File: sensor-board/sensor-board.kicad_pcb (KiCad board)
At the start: 2 copper layers, 11 parts, among them Q1 DMG3415U-7, U1 MCP73831-3-OT, U2 Arduino-nano-BLE-33, U3 SCD40-D-R2, U4 SGP40-D-R4

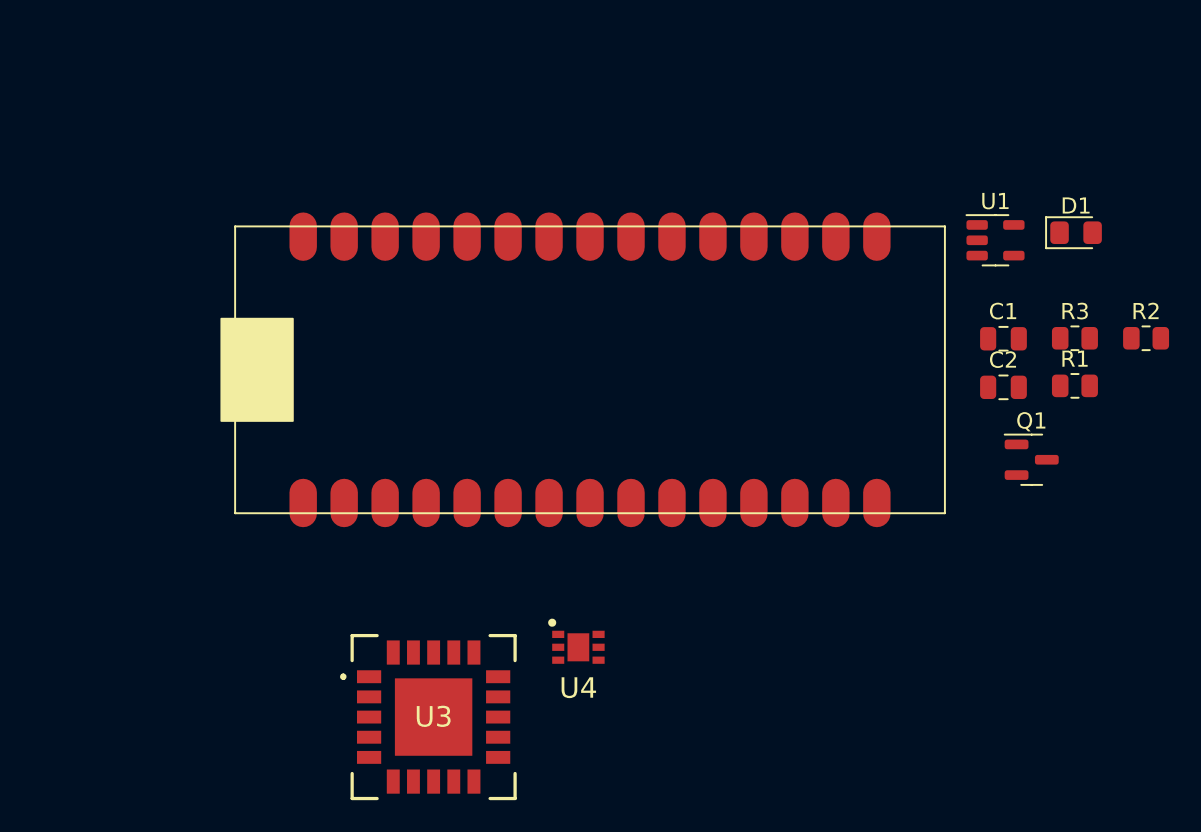
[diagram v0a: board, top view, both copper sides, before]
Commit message: update sensors and sensorBoard
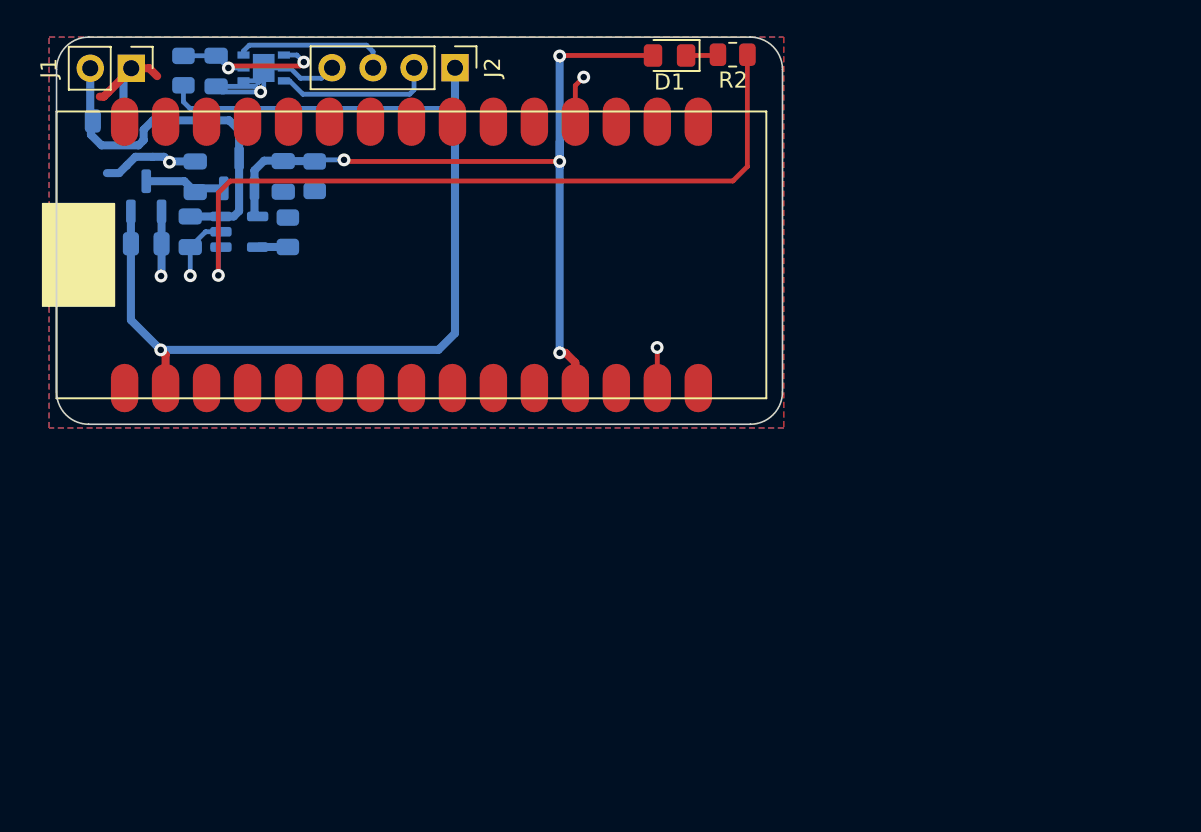
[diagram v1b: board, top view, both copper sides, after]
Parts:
- added C3: 10uF, Capacitor_SMD:C_0805_2012Metric, B.Cu at (134.1, 64.6)
- added C4: 10uF, Capacitor_SMD:C_0805_2012Metric, B.Cu at (123.2, 61.2)
- added C5: 10uF, Capacitor_SMD:C_0805_2012Metric, B.Cu at (125.6, 68.8)
- added C6: 1uF, Capacitor_SMD:C_0805_2012Metric, B.Cu at (129.9, 58.1)
- added J1: Batt, Connector_PinHeader_2.54mm:PinHeader_1x02_P2.54mm_Vertical, F.Cu at (124.6, 57.9)
- added J2: I2C, Connector_PinHeader_2.54mm:PinHeader_1x04_P2.54mm_Vertical, F.Cu at (144.7, 57.9)
- added R4: 4.7R, Resistor_SMD:R_0805_2012Metric, B.Cu at (127.9, 58.1)
- C1, C2, Q1, R1, R3, U1, U4: moved to B.Cu
- U3: value SCD40-D-R2 -> MCP1700T-3102; footprint hack-it-back:SCD40DR2 -> Package_TO_SOT_SMD:SOT-23; moved to B.Cu
- moved Q1 52.2 mm to (131.3, 64.4), turned to 90 degrees
- moved C2 51.8 mm to (128.6, 64.7), turned to 90 degrees
- moved C1 50.8 mm to (128.3, 68.1), turned to -90 degrees
- moved R1 49.7 mm to (134.3, 68.1), turned to 90 degrees
- moved R3 48.2 mm to (136.0, 64.6), turned to -90 degrees
- moved U1 46.9 mm to (131.3, 68.1)
- moved U4 40.9 mm to (132.8, 57.9), turned to 180 degrees
- moved U3 36.9 mm to (125.6, 65.9), turned to 90 degrees
- moved R2 31.1 mm to (161.9, 57.1), turned to 180 degrees
- moved D1 27.5 mm to (158.0, 57.1), turned to 180 degrees
- moved U2 13.2 mm to (142.0, 69.5)
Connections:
- U2 pad 15: VDD -> unconnected-(U2-Pad15)
- U2 pad 19: unconnected-(U2-Pad19) -> GND
- U2 pad 2: unconnected-(U2-Pad2) -> +3V3
- U3 pad 1: (no net) -> GND
- U3 pad 2: (no net) -> +3V3
- U3 pad 3: (no net) -> VDD
- U4 pad 1: unconnected-(U4-Pad1) -> Net-(U4-Pad1)
- U4 pad 2: unconnected-(U4-Pad2) -> GND
- U4 pad 3: unconnected-(U4-Pad3) -> /SDA
- U4 pad 4: unconnected-(U4-Pad4) -> GND
- U4 pad 5: unconnected-(U4-Pad5) -> Net-(U4-Pad1)
- U4 pad 6: unconnected-(U4-Pad6) -> /SCL
- U4 pad 7: unconnected-(U4-Pad7) -> GND
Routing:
- net +3V3: track 0.00 -> 67.8 mm, vias 0 -> 1
- net VBUS: track 0.00 -> 57.3 mm, vias 0 -> 4
- net Net-(R2-Pad1): track 0.00 -> 47.3 mm, vias 0 -> 1
- net GND: track 0.00 -> 41.8 mm, vias 0 -> 6
- net +BATT: track 0.00 -> 23.2 mm
- net Net-(U4-Pad1): track 0.00 -> 10.3 mm, vias 0 -> 2
- net /SDA: track 0.00 -> 9.89 mm
- net /SCL: track 0.00 -> 9.60 mm
- net VDD: track 0.00 -> 5.18 mm
- net Net-(D1-Pad1): track 0.00 -> 2.00 mm
- net Net-(R1-Pad1): track 0.00 -> 1.88 mm
- added copper zone on B.Cu, net GND
- added copper zone on F.Cu, net GND
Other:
- board outline added: 45 x 24 mm

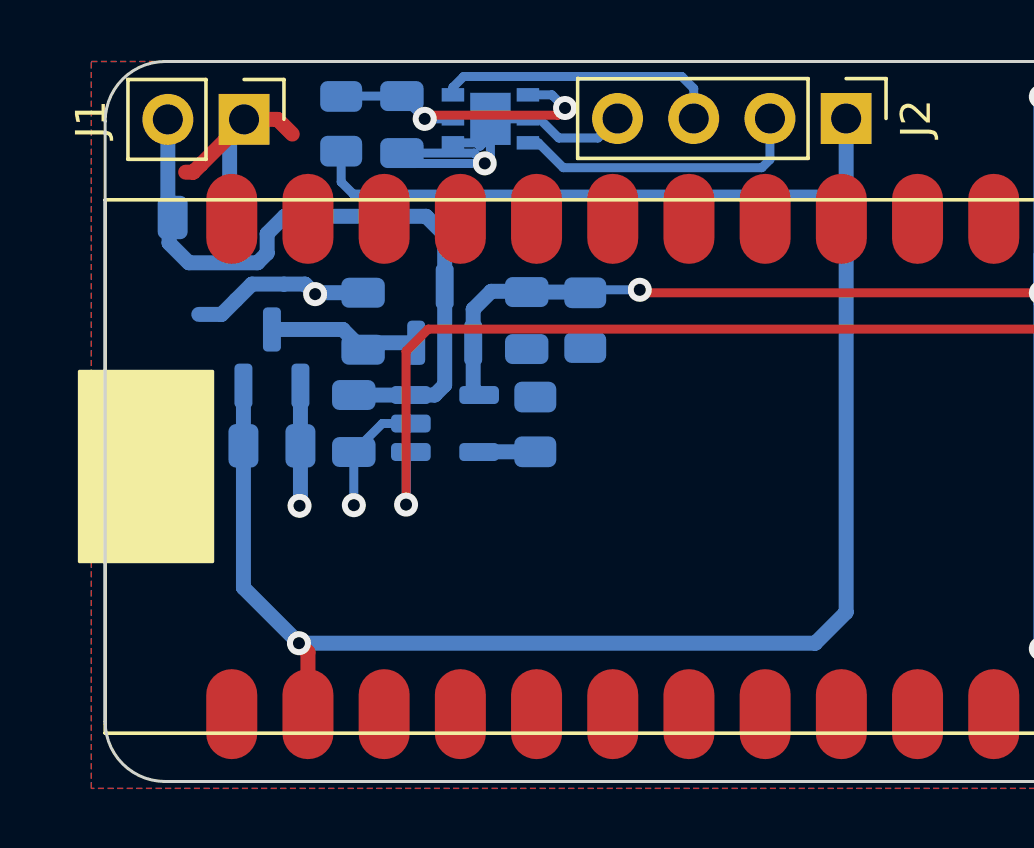
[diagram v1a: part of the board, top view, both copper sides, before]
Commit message: update pins sensor board
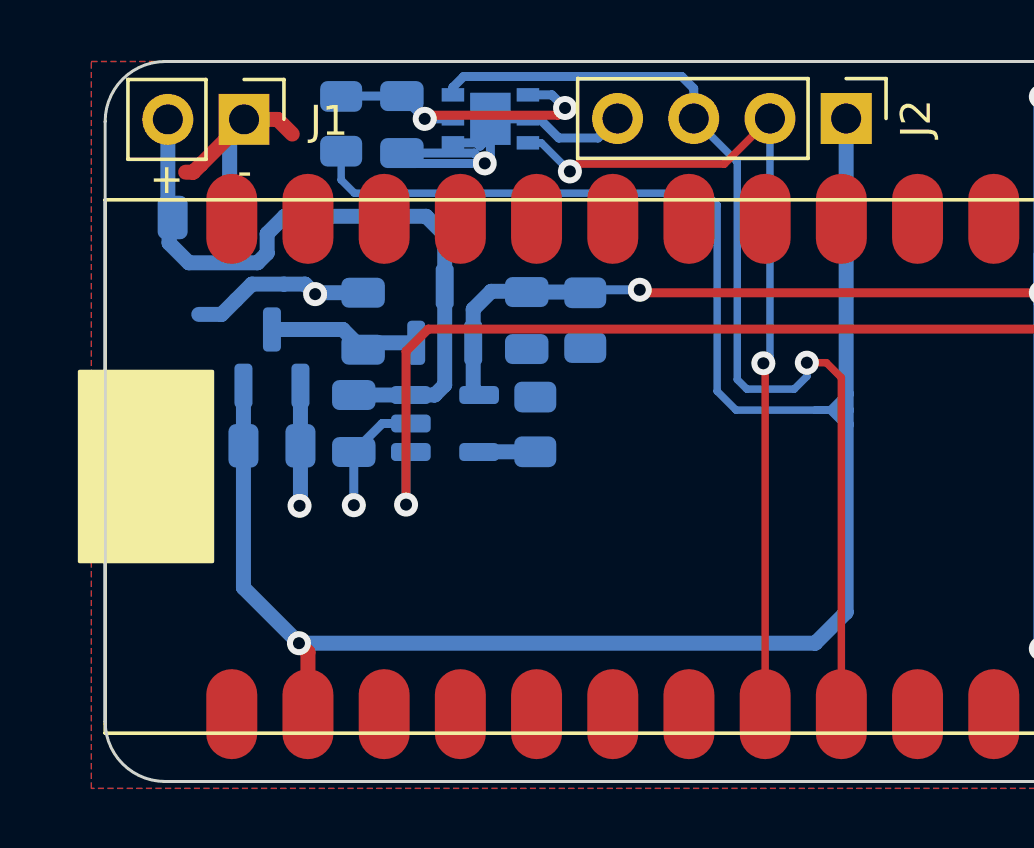
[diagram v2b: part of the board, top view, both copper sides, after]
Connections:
- U2 pad 8: unconnected-(U2-Pad8) -> /SDA
- U2 pad 9: unconnected-(U2-Pad9) -> /SCL
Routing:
- net /SCL: track 9.60 -> 34.6 mm, vias 0 -> 1
- net /SDA: track 9.89 -> 29.2 mm, vias 0 -> 2
- net +3V3: track 67.8 -> 75.6 mm
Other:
- board text added: "+"
- board text added: "-"

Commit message: update sensor board v1.0
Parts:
- moved D1 31.6 mm to (126.4, 57.3)
- moved R2 31.4 mm to (130.5, 57.4)
- moved R4 28.9 mm to (153.6, 71.3), turned to 0 degrees
- moved C6 26.2 mm to (153.6, 69.3), turned to 0 degrees
- moved U4 22.2 mm to (153.4, 66.3), turned to -90 degrees
- moved C4 15.4 mm to (138.6, 61.0), turned to 180 degrees
- moved J1 12.9 mm to (137.5, 57.8), turned to 90 degrees
- moved J2 12.8 mm to (157.5, 58.0)
- moved C1 9.29 mm to (137.4, 69.7)
- moved C2 9.29 mm to (137.7, 66.3)
- moved C5 9.29 mm to (134.7, 70.5)
- moved Q1 9.29 mm to (140.5, 66.1)
- moved R1 9.29 mm to (143.5, 69.8)
- moved R3 9.29 mm to (145.1, 66.3)
- moved U1 9.29 mm to (140.5, 69.7)
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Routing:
- net Net-(R2-Pad1): track 47.3 -> 25.0 mm, vias 1 -> 3
- net GND: track 41.8 -> 29.5 mm, vias 6 -> 37
- net +BATT: track 23.2 -> 14.2 mm
- net VBUS: track 57.3 -> 50.8 mm
- net /SDA: track 29.2 -> 33.1 mm, vias 2 -> 1
- net Net-(C6-Pad1): track 10.3 -> 13.5 mm
- net /SCL: track 34.6 -> 33.7 mm, vias 1 -> 2
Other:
- board size 45 x 24 mm -> 38 x 24 mm
- board text added: "Sensor Board"
- board text added: "v1.0"
